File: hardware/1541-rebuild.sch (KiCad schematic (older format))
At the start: 12 parts, among them IC1 ATMEGA1284P-P, J1 ISP, J2 KEYS, J3 EXT_5V, J4 RESET CONN, J5 PC7, SW1 RESET, X1 24Mhz

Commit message: ERC Check Fehler behoben. GND + +5V PIN auf Power Out gestellt.
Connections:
- wire segments 125 -> 113
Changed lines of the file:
@@
 NoConn ~ 3600 3200
 $Comp
-L GND #PWR10
+L GND #PWR01
 U 1 1 55F7D4A6
 P 2000 3200
-F 0 "#PWR10" H 2000 2950 50  0001 C CNN
+F 0 "#PWR01" H 2000 2950 50  0001 C CNN
 F 1 "GND" H 2000 3050 50  0000 C CNN
 F 2 "" H 2000 3200 60  0000 C CNN
@@
 $EndComp
 $Comp
-L +5V #PWR8
+L +5V #PWR02
 U 1 1 55F7D4E4
 P 2000 2900
-F 0 "#PWR8" H 2000 2750 50  0001 C CNN
+F 0 "#PWR02" H 2000 2750 50  0001 C CNN
 F 1 "+5V" H 2000 3040 50  0000 C CNN
 F 2 "" H 2000 2900 60  0000 C CNN
@@
 NoConn ~ 4100 2500
 $Comp
-L GND #PWR13
+L GND #PWR03
 U 1 1 55F7EFD4
 P 5000 5950
-F 0 "#PWR13" H 5000 5700 50  0001 C CNN
+F 0 "#PWR03" H 5000 5700 50  0001 C CNN
 F 1 "GND" H 5000 5800 50  0000 C CNN
 F 2 "" H 5000 5950 60  0000 C CNN
@@
 $EndComp
 $Comp
-L +5V #PWR5
+L +5V #PWR04
 U 1 1 55F7F7C2
 P 5000 1650
-F 0 "#PWR5" H 5000 1500 50  0001 C CNN
+F 0 "#PWR04" H 5000 1500 50  0001 C CNN
 F 1 "+5V" H 5000 1790 50  0000 C CNN
 F 2 "" H 5000 1650 60  0000 C CNN
@@
 $EndComp
 $Comp
-L +5V #PWR7
+L +5V #PWR05
 U 1 1 55F7ED10
 P 3500 2100
-F 0 "#PWR7" H 3500 1950 50  0001 C CNN
+F 0 "#PWR05" H 3500 1950 50  0001 C CNN
 F 1 "+5V" H 3500 2240 50  0000 C CNN
 F 2 "" H 3500 2100 60  0000 C CNN
@@
 $EndComp
 $Comp
-L +5V #PWR3
+L +5V #PWR06
 U 1 1 55F800FF
 P 1500 1050
-F 0 "#PWR3" H 1500 900 50  0001 C CNN
+F 0 "#PWR06" H 1500 900 50  0001 C CNN
 F 1 "+5V" H 1500 1190 50  0000 C CNN
 F 2 "" H 1500 1050 60  0000 C CNN
@@
 $EndComp
 $Comp
-L GND #PWR2
+L GND #PWR07
 U 1 1 55F80221
 P 1200 1050
-F 0 "#PWR2" H 1200 800 50  0001 C CNN
+F 0 "#PWR07" H 1200 800 50  0001 C CNN
 F 1 "GND" H 1200 900 50  0000 C CNN
 F 2 "" H 1200 1050 60  0000 C CNN
@@
 $EndSheet
 Wire Wire Line
-	2000 2900 2100 2900
-Wire Wire Line
-	2100 2900 2200 2900
+	2000 2900 2200 2900
 Connection ~ 2100 2900
 Wire Wire Line
-	2000 3200 2100 3200
-Wire Wire Line
-	2100 3200 2200 3200
+	2000 3200 2200 3200
 Connection ~ 2100 3200
 Wire Wire Line
 	4900 5800 4900 5900
 Wire Wire Line
-	4900 5900 5000 5900
-Wire Wire Line
-	5000 5900 5100 5900
+	4900 5900 5100 5900
 Wire Wire Line
 	5000 5900 5000 5950
@@
 	4900 1800 4900 1700
 Wire Wire Line
-	4900 1700 5000 1700
-Wire Wire Line
-	5000 1700 5100 1700
+	4900 1700 5100 1700
 Wire Wire Line
 	5000 1700 5000 1650
@@
 	3650 2100 3500 2100
 Wire Wire Line
-	3950 2100 4050 2100
-Wire Wire Line
-	4050 2100 4100 2100
-Wire Wire Line
-	1200 1050 1200 1250
-Wire Wire Line
-	1200 1250 1200 1550
+	3950 2100 4100 2100
+Wire Wire Line
+	1200 1050 1200 1550
 Connection ~ 1200 1250
 Wire Wire Line
-	1500 1050 1500 1250
-Wire Wire Line
-	1500 1250 1500 1550
+	1500 1050 1500 1550
 Connection ~ 1500 1250
 Wire Wire Line
@@
 	6100 3400 7550 3400
 Wire Wire Line
-	6100 3500 7350 3500
-Wire Wire Line
-	7350 3500 7550 3500
-Wire Wire Line
-	6100 3600 7150 3600
-Wire Wire Line
-	7150 3600 7550 3600
-Wire Wire Line
-	6100 3700 7250 3700
-Wire Wire Line
-	7250 3700 7550 3700
+	6100 3500 7550 3500
+Wire Wire Line
+	6100 3600 7550 3600
+Wire Wire Line
+	6100 3700 7550 3700
 Wire Wire Line
 	6100 3300 6550 3300
@@
 	4050 2100 4050 1000
 Wire Wire Line
-	3950 1000 4050 1000
-Wire Wire Line
-	4050 1000 7400 1000
-Wire Wire Line
-	7400 1000 10650 1000
+	3950 1000 10650 1000
 Wire Wire Line
 	7400 1000 7400 1700
@@
 Connection ~ 4050 2100
 $Comp
-L +5V #PWR4
+L +5V #PWR08
 U 1 1 58409984
 P 8250 1450
-F 0 "#PWR4" H 8250 1300 50  0001 C CNN
+F 0 "#PWR08" H 8250 1300 50  0001 C CNN
 F 1 "+5V" H 8250 1590 50  0000 C CNN
 F 2 "" H 8250 1450 60  0000 C CNN
@@
 	8250 1500 8250 1450
 $Comp
-L GND #PWR6
+L GND #PWR09
 U 1 1 58409C3B
 P 8250 1750
-F 0 "#PWR6" H 8250 1500 50  0001 C CNN
+F 0 "#PWR09" H 8250 1500 50  0001 C CNN
 F 1 "GND" H 8250 1600 50  0000 C CNN
 F 2 "" H 8250 1750 60  0000 C CNN
@@
 Connection ~ 4050 1000
 $Comp
-L GND #PWR1
+L GND #PWR010
 U 1 1 5ADB9F66
 P 3100 1000
-F 0 "#PWR1" H 3100 1000 30  0001 C CNN
+F 0 "#PWR010" H 3100 1000 30  0001 C CNN
 F 1 "GND" H 3100 930 30  0001 C CNN
 F 2 "" H 3100 1000 60  0001 C CNN
@@
 $EndComp
 $Comp
-L GND #PWR9
+L GND #PWR011
 U 1 1 5AEE4F44
 P 9850 3150
-F 0 "#PWR9" H 9850 2900 50  0001 C CNN
+F 0 "#PWR011" H 9850 2900 50  0001 C CNN
 F 1 "GND" H 9850 3000 50  0000 C CNN
 F 2 "" H 9850 3150 60  0000 C CNN
@@
 $EndComp
 $Comp
-L GND #PWR12
+L GND #PWR012
 U 1 1 5AEF6E70
 P 1550 4700
-F 0 "#PWR12" H 1550 4450 50  0001 C CNN
+F 0 "#PWR012" H 1550 4450 50  0001 C CNN
 F 1 "GND" H 1550 4550 50  0000 C CNN
 F 2 "" H 1550 4700 60  0000 C CNN
@@
 $EndComp
 $Comp
-L +5V #PWR11
+L +5V #PWR013
 U 1 1 5AEF757D
 P 1250 4700
-F 0 "#PWR11" H 1250 4550 50  0001 C CNN
+F 0 "#PWR013" H 1250 4550 50  0001 C CNN
 F 1 "+5V" H 1250 4840 50  0000 C CNN
 F 2 "" H 1250 4700 60  0000 C CNN

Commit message: Allen Bauteilen Footprints zugeordnet.
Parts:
- J1: footprint (none) -> w_conn_strip:vasch_strip_3x2
- J2: footprint (none) -> Pin_Headers:Pin_Header_Straight_1x04_Pitch2.54mm
- J3, J4: footprint (none) -> Pin_Headers:Pin_Header_Straight_1x02_Pitch2.54mm
- J5: footprint (none) -> Pin_Headers:Pin_Header_Straight_1x01_Pitch2.54mm
- R1: footprint Resistors_ThroughHole:Resistor_Horizontal_RM10mm -> Discret:R4-5
- SW1: footprint Buttons_Switches_THT:SW_PUSH-12mm -> Buttons_Switches_THT:SW_PUSH_6mm_h5mm
- X1: footprint Oscillators:KXO-200_LargePads -> Oscillators:Oscillator_DIP-14_LargePads
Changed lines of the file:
@@
 F 0 "X1" H 2900 3350 70  0000 C CNN
 F 1 "24Mhz" H 2900 3050 70  0000 C CNN
-F 2 "Oscillators:KXO-200_LargePads" H 2900 3050 60  0001 C CNN
+F 2 "Oscillators:Oscillator_DIP-14_LargePads" H 2900 3050 60  0001 C CNN
 F 3 "" H 2900 3050 60  0000 C CNN
 	1    2900 3050
@@
 F 0 "R1" V 3880 2100 50  0000 C CNN
 F 1 "10k" V 3800 2100 50  0000 C CNN
-F 2 "Resistors_ThroughHole:Resistor_Horizontal_RM10mm" V 3730 2100 30  0001 C CNN
+F 2 "Discret:R4-5" V 3730 2100 30  0001 C CNN
 F 3 "" H 3800 2100 30  0000 C CNN
 	1    3800 2100
@@
 F 0 "SW1" H 3800 1110 50  0000 C CNN
 F 1 "RESET" H 3650 920 50  0000 C CNN
-F 2 "Buttons_Switches_THT:SW_PUSH-12mm" H 3650 1000 60  0001 C CNN
+F 2 "Buttons_Switches_THT:SW_PUSH_6mm_h5mm" H 3650 1000 60  0001 C CNN
 F 3 "" H 3650 1000 60  0000 C CNN
 	1    3650 1000
@@
 F 0 "J5" H 6200 6050 50  0000 C CNN
 F 1 "PC7" H 6200 5850 50  0000 C CNN
-F 2 "" H 6200 5950 50  0001 C CNN
+F 2 "Pin_Headers:Pin_Header_Straight_1x01_Pitch2.54mm" H 6200 5950 50  0001 C CNN
 F 3 "" H 6200 5950 50  0001 C CNN
 	1    6200 5950
@@
 F 0 "J2" H 10200 3150 50  0000 C CNN
 F 1 "KEYS" H 10200 2650 50  0000 C CNN
-F 2 "" H 10200 2950 50  0001 C CNN
+F 2 "Pin_Headers:Pin_Header_Straight_1x04_Pitch2.54mm" H 10200 2950 50  0001 C CNN
 F 3 "" H 10200 2950 50  0001 C CNN
 	1    10200 2950
@@
 F 0 "J1" H 7850 1800 50  0000 C CNN
 F 1 "ISP" H 7850 1400 50  0000 C CNN
-F 2 "" H 7800 1600 50  0001 C CNN
+F 2 "w_conn_strip:vasch_strip_3x2" H 7800 1600 50  0001 C CNN
 F 3 "" H 7800 1600 50  0001 C CNN
 	1    7800 1600
@@
 F 0 "J4" H 9400 4650 50  0000 C CNN
 F 1 "RESET CONN" H 9400 4350 50  0000 C CNN
-F 2 "" H 9400 4550 50  0001 C CNN
+F 2 "Pin_Headers:Pin_Header_Straight_1x02_Pitch2.54mm" H 9400 4550 50  0001 C CNN
 F 3 "" H 9400 4550 50  0001 C CNN
 	1    9400 4550
@@
 F 0 "J3" H 1350 4450 50  0000 C CNN
 F 1 "EXT_5V" H 1350 4150 50  0000 C CNN
-F 2 "" H 1350 4350 50  0001 C CNN
+F 2 "Pin_Headers:Pin_Header_Straight_1x02_Pitch2.54mm" H 1350 4350 50  0001 C CNN
 F 3 "" H 1350 4350 50  0001 C CNN
 	1    1350 4350

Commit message: - Hardware nochmal angepasst - erstes Layout erstellt - Schaltplan auf Rev.1.3.4 gesetzt
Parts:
- removed J5: PC7, Pin_Headers:Pin_Header_Straight_1x01_Pitch2.54mm, symbol Conn_01x01
- added J5: PC7, Pin_Headers:Pin_Header_Straight_1x02_Pitch2.54mm, symbol Conn_01x02
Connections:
- wire segments 113 -> 115
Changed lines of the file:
@@
 EESchema Schematic File Version 2
+LIBS:power
+LIBS:ka_library
 LIBS:1541-rebuild-rescue
-LIBS:power
 LIBS:device
 LIBS:transistors
@@
 LIBS:w_transistor
 LIBS:w_vacuum
-LIBS:kattanek
 LIBS:1541-rebuild-cache
 EELAYER 25 0
@@
 Sheet 1 4
 Title "1541-rebuid"
-Date "2018-05-06"
-Rev "1.3.3"
+Date "2018-05-08"
+Rev "1.3.4"
 Comp ""
 Comment1 "Erstellt von: Thorsten Kattanek"
@@
 NoConn ~ 3600 3200
 $Comp
-L GND #PWR01
-U 1 1 55F7D4A6
-P 2000 3200
-F 0 "#PWR01" H 2000 2950 50  0001 C CNN
-F 1 "GND" H 2000 3050 50  0000 C CNN
-F 2 "" H 2000 3200 60  0000 C CNN
-F 3 "" H 2000 3200 60  0000 C CNN
-	1    2000 3200
-	0    1    1    0
-$EndComp
-$Comp
-L +5V #PWR02
+L +5V #PWR01
 U 1 1 55F7D4E4
 P 2000 2900
-F 0 "#PWR02" H 2000 2750 50  0001 C CNN
+F 0 "#PWR01" H 2000 2750 50  0001 C CNN
 F 1 "+5V" H 2000 3040 50  0000 C CNN
 F 2 "" H 2000 2900 60  0000 C CNN
@@
 NoConn ~ 4100 2500
 $Comp
-L GND #PWR03
-U 1 1 55F7EFD4
-P 5000 5950
-F 0 "#PWR03" H 5000 5700 50  0001 C CNN
-F 1 "GND" H 5000 5800 50  0000 C CNN
-F 2 "" H 5000 5950 60  0000 C CNN
-F 3 "" H 5000 5950 60  0000 C CNN
-	1    5000 5950
-	1    0    0    -1
-$EndComp
-$Comp
-L +5V #PWR04
+L +5V #PWR02
 U 1 1 55F7F7C2
 P 5000 1650
-F 0 "#PWR04" H 5000 1500 50  0001 C CNN
+F 0 "#PWR02" H 5000 1500 50  0001 C CNN
 F 1 "+5V" H 5000 1790 50  0000 C CNN
 F 2 "" H 5000 1650 60  0000 C CNN
@@
 $EndComp
 $Comp
-L +5V #PWR05
+L +5V #PWR03
 U 1 1 55F7ED10
 P 3500 2100
-F 0 "#PWR05" H 3500 1950 50  0001 C CNN
+F 0 "#PWR03" H 3500 1950 50  0001 C CNN
 F 1 "+5V" H 3500 2240 50  0000 C CNN
 F 2 "" H 3500 2100 60  0000 C CNN
@@
 $EndComp
 $Comp
-L +5V #PWR06
+L +5V #PWR04
 U 1 1 55F800FF
 P 1500 1050
-F 0 "#PWR06" H 1500 900 50  0001 C CNN
+F 0 "#PWR04" H 1500 900 50  0001 C CNN
 F 1 "+5V" H 1500 1190 50  0000 C CNN
 F 2 "" H 1500 1050 60  0000 C CNN
@@
 	1    1500 1050
 	1    0    0    -1
-$EndComp
-$Comp
-L GND #PWR07
-U 1 1 55F80221
-P 1200 1050
-F 0 "#PWR07" H 1200 800 50  0001 C CNN
-F 1 "GND" H 1200 900 50  0000 C CNN
-F 2 "" H 1200 1050 60  0000 C CNN
-F 3 "" H 1200 1050 60  0000 C CNN
-	1    1200 1050
-	-1   0    0    1
 $EndComp
 Text Notes 750  750  0    60   ~ 0
@@
 Connection ~ 4050 2100
 $Comp
-L +5V #PWR08
+L +5V #PWR05
 U 1 1 58409984
 P 8250 1450
-F 0 "#PWR08" H 8250 1300 50  0001 C CNN
+F 0 "#PWR05" H 8250 1300 50  0001 C CNN
 F 1 "+5V" H 8250 1590 50  0000 C CNN
 F 2 "" H 8250 1450 60  0000 C CNN
@@
 Wire Wire Line
 	8250 1500 8250 1450
-$Comp
-L GND #PWR09
-U 1 1 58409C3B
-P 8250 1750
-F 0 "#PWR09" H 8250 1500 50  0001 C CNN
-F 1 "GND" H 8250 1600 50  0000 C CNN
-F 2 "" H 8250 1750 60  0000 C CNN
-F 3 "" H 8250 1750 60  0000 C CNN
-	1    8250 1750
-	1    0    0    -1
-$EndComp
 Wire Wire Line
 	8100 1700 8250 1700
@@
 Connection ~ 7350 3500
 Wire Wire Line
-	6200 4600 6200 5750
-Wire Wire Line
-	6200 4600 6100 4600
+	6100 4600 6250 4600
 Wire Wire Line
 	10650 1000 10650 4900
@@
 $EndComp
 Connection ~ 4050 1000
-$Comp
-L GND #PWR010
-U 1 1 5ADB9F66
-P 3100 1000
-F 0 "#PWR010" H 3100 1000 30  0001 C CNN
-F 1 "GND" H 3100 930 30  0001 C CNN
-F 2 "" H 3100 1000 60  0001 C CNN
-F 3 "" H 3100 1000 60  0001 C CNN
-	1    3100 1000
-	0    1    1    0
-$EndComp
 Wire Wire Line
 	3100 1000 3350 1000
-$Comp
-L Conn_01x01 J5
-U 1 1 5AED8BA4
-P 6200 5950
-F 0 "J5" H 6200 6050 50  0000 C CNN
-F 1 "PC7" H 6200 5850 50  0000 C CNN
-F 2 "Pin_Headers:Pin_Header_Straight_1x01_Pitch2.54mm" H 6200 5950 50  0001 C CNN
-F 3 "" H 6200 5950 50  0001 C CNN
-	1    6200 5950
-	0    1    1    0
-$EndComp
 $Comp
 L Conn_01x04 J2
@@
 	1    10200 2950
 	1    0    0    -1
-$EndComp
-$Comp
-L GND #PWR011
-U 1 1 5AEE4F44
-P 9850 3150
-F 0 "#PWR011" H 9850 2900 50  0001 C CNN
-F 1 "GND" H 9850 3000 50  0000 C CNN
-F 2 "" H 9850 3150 60  0000 C CNN
-F 3 "" H 9850 3150 60  0000 C CNN
-	1    9850 3150
-	0    1    1    0
 $EndComp
 Wire Wire Line
@@
 $EndComp
 $Comp
-L GND #PWR012
-U 1 1 5AEF6E70
-P 1550 4700
-F 0 "#PWR012" H 1550 4450 50  0001 C CNN
-F 1 "GND" H 1550 4550 50  0000 C CNN
-F 2 "" H 1550 4700 60  0000 C CNN
-F 3 "" H 1550 4700 60  0000 C CNN
-	1    1550 4700
-	0    -1   -1   0
-$EndComp
-$Comp
-L +5V #PWR013
+L +5V #PWR06
 U 1 1 5AEF757D
 P 1250 4700
-F 0 "#PWR013" H 1250 4550 50  0001 C CNN
+F 0 "#PWR06" H 1250 4550 50  0001 C CNN
 F 1 "+5V" H 1250 4840 50  0000 C CNN
 F 2 "" H 1250 4700 60  0000 C CNN
@@
 Wire Wire Line
 	3600 2900 4100 2900
+$Comp
+L GND #PWR07
+U 1 1 5AF09AC0
+P 1200 1050
+F 0 "#PWR07" H 1200 800 50  0001 C CNN
+F 1 "GND" H 1200 900 50  0000 C CNN
+F 2 "" H 1200 1050 50  0001 C CNN
+F 3 "" H 1200 1050 50  0001 C CNN
+	1    1200 1050
+	-1   0    0    1
+$EndComp
+$Comp
+L GND #PWR08
+U 1 1 5AF09DC8
+P 3100 1000
+F 0 "#PWR08" H 3100 750 50  0001 C CNN
+F 1 "GND" H 3100 850 50  0000 C CNN
+F 2 "" H 3100 1000 50  0001 C CNN
+F 3 "" H 3100 1000 50  0001 C CNN
+	1    3100 1000
+	0    1    1    0
+$EndComp
+$Comp
+L GND #PWR09
+U 1 1 5AF0A3CF
+P 2000 3200
+F 0 "#PWR09" H 2000 2950 50  0001 C CNN
+F 1 "GND" H 2000 3050 50  0000 C CNN
+F 2 "" H 2000 3200 50  0001 C CNN
+F 3 "" H 2000 3200 50  0001 C CNN
+	1    2000 3200
+	0    1    1    0
+$EndComp
+$Comp
+L GND #PWR010
+U 1 1 5AF0A9E7
+P 1550 4700
+F 0 "#PWR010" H 1550 4450 50  0001 C CNN
+F 1 "GND" H 1550 4550 50  0000 C CNN
+F 2 "" H 1550 4700 50  0001 C CNN
+F 3 "" H 1550 4700 50  0001 C CNN
+	1    1550 4700
+	0    -1   -1   0
+$EndComp
+$Comp
+L GND #PWR011
+U 1 1 5AF0ADEC
+P 5000 5950
+F 0 "#PWR011" H 5000 5700 50  0001 C CNN
+F 1 "GND" H 5000 5800 50  0000 C CNN
+F 2 "" H 5000 5950 50  0001 C CNN
+F 3 "" H 5000 5950 50  0001 C CNN
+	1    5000 5950
+	1    0    0    -1
+$EndComp
+$Comp
+L GND #PWR012
+U 1 1 5AF0B2ED
+P 8250 1750
+F 0 "#PWR012" H 8250 1500 50  0001 C CNN
+F 1 "GND" H 8250 1600 50  0000 C CNN
+F 2 "" H 8250 1750 50  0001 C CNN
+F 3 "" H 8250 1750 50  0001 C CNN
+	1    8250 1750
+	1    0    0    -1
+$EndComp
+$Comp
+L GND #PWR013
+U 1 1 5AF0B7EE
+P 9850 3150
+F 0 "#PWR013" H 9850 2900 50  0001 C CNN
+F 1 "GND" H 9850 3000 50  0000 C CNN
+F 2 "" H 9850 3150 50  0001 C CNN
+F 3 "" H 9850 3150 50  0001 C CNN
+	1    9850 3150
+	0    1    1    0
+$EndComp
+$Comp
+L Conn_01x02 J5
+U 1 1 5AF1C880
+P 6250 6200
+F 0 "J5" H 6250 6300 50  0000 C CNN
+F 1 "PC7" H 6250 6000 50  0000 C CNN
+F 2 "Pin_Headers:Pin_Header_Straight_1x02_Pitch2.54mm" H 6250 6200 50  0001 C CNN
+F 3 "" H 6250 6200 50  0001 C CNN
+	1    6250 6200
+	0    1    1    0
+$EndComp
+Wire Wire Line
+	6250 4600 6250 6000
+$Comp
+L GND #PWR014
+U 1 1 5AF1E3E7
+P 6050 5950
+F 0 "#PWR014" H 6050 5700 50  0001 C CNN
+F 1 "GND" H 6050 5800 50  0000 C CNN
+F 2 "" H 6050 5950 50  0001 C CNN
+F 3 "" H 6050 5950 50  0001 C CNN
+	1    6050 5950
+	0    1    1    0
+$EndComp
+Wire Wire Line
+	6050 5950 6150 5950
+Wire Wire Line
+	6150 5950 6150 6000
 $EndSCHEMATC

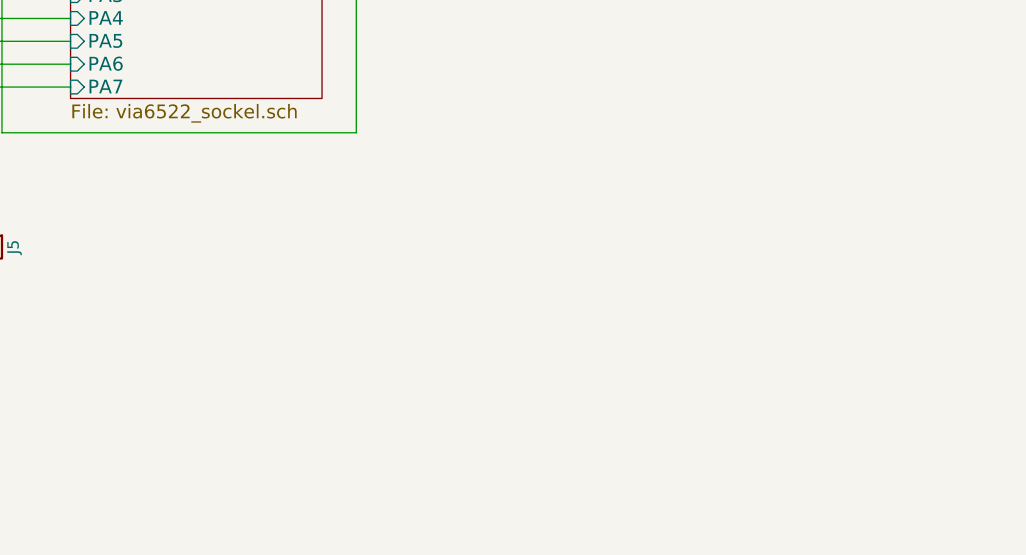
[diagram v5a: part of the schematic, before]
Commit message: Bezugsquellen für den SD Slot im Schaltplan hinzugefügt.
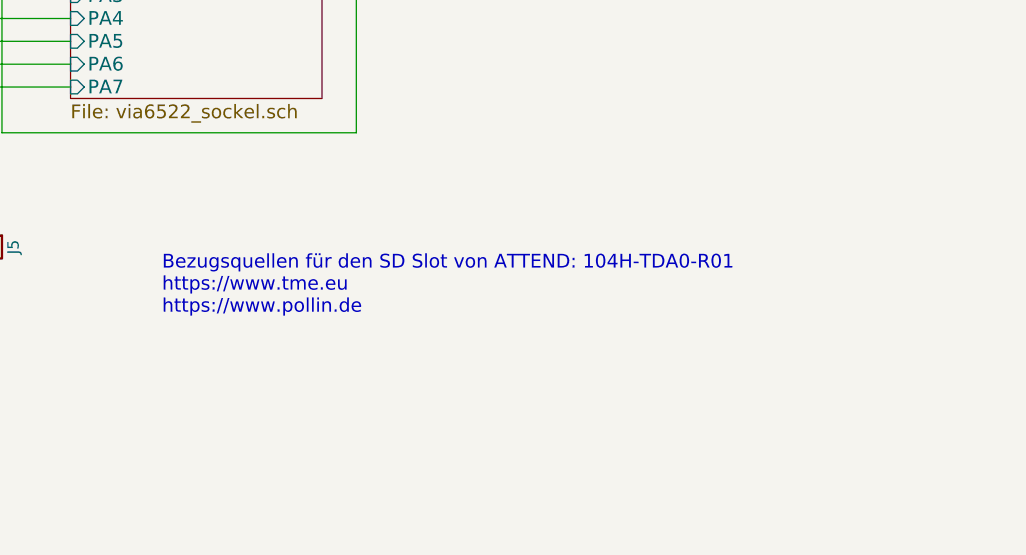
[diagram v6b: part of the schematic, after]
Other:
- note added: "Bezugsquellen für den SD Slot von ATTEND: 104H-TDA0-R01\nhttps://www.tme.eu\nhttps://www.pollin.de\n"
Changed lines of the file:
@@
 Sheet 1 4
 Title "1541-rebuid"
-Date "2018-05-11"
+Date "2018-05-16"
 Rev "1.3.5"
 Comp ""
@@
 Wire Wire Line
 	6150 5950 6150 6000
+Text Notes 7000 6500 0    60   ~ 0
+Bezugsquellen für den SD Slot von ATTEND: 104H-TDA0-R01\nhttps://www.tme.eu\nhttps://www.pollin.de\n
 $EndSCHEMATC

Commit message: Hardware Projekt knovertiert von KiCad 4 -> KiCad 5 - Schaltplan angepasst - neues Detailfoto hinzugefügt - Footprints neu zugeordnet, somit ist auch wieder eine 3D Darstellung möglich - Readme.md angepasst
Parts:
- C1, C2, C3: footprint w_capacitors:cnp_3mm_disc -> Capacitor_THT:C_Disc_D5.1mm_W3.2mm_P5.00mm; symbol C -> Device:C
- IC1: footprint w_pth_circuits:dil_40-600_socket -> Package_DIP:DIP-40_W15.24mm_Socket_LongPads; symbol ATMEGA1284P-P -> MCU_Microchip_ATmega:ATmega1284P-PU
- J1: footprint w_conn_strip:vasch_strip_3x2 -> Connector_IDC:IDC-Header_2x03_P2.54mm_Vertical; symbol Conn_02x03_Odd_Even -> Connector_Generic:Conn_02x03_Odd_Even
- J2: footprint Pin_Headers:Pin_Header_Straight_1x04_Pitch2.54mm -> Connector_PinHeader_2.54mm:PinHeader_1x04_P2.54mm_Vertical; symbol Conn_01x04 -> Connector_Generic:Conn_01x04
- J3, J4, J5: footprint Pin_Headers:Pin_Header_Straight_1x02_Pitch2.54mm -> Connector_PinHeader_2.54mm:PinHeader_1x02_P2.54mm_Vertical; symbol Conn_01x02 -> Connector_Generic:Conn_01x02
- R1: footprint Discret:R4-5 -> Resistor_THT:R_Axial_DIN0207_L6.3mm_D2.5mm_P10.16mm_Horizontal; symbol R -> Device:R
- SW1: footprint Buttons_Switches_THT:SW_PUSH_6mm_h5mm -> Button_Switch_THT:SW_PUSH_6mm_H5mm; symbol SW_PUSH-RESCUE-1541-rebuild -> Switch:SW_Push
- X1: footprint Oscillators:Oscillator_DIP-14_LargePads -> Oscillator:Oscillator_DIP-14_LargePads; symbol TCXO3-RESCUE-1541-rebuild -> Oscillator:TCXO-14
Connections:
- net LCD Display/D0 renamed LCD Display/D4
- net LCD Display/D1 renamed LCD Display/D5
- net LCD Display/D2 renamed LCD Display/D6
- net LCD Display/D3 renamed LCD Display/D7
- no-connect marks 3 -> 2
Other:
- note added: "Am meiner 1541II Platine (ASSY NO 345003 REV 9) habe ich folgende modifiktionen durchgeführt:\n- PIN 42 von U10 (Gate Array 251828) von Platine getrennt (BYTE READY)\n- U8 (VIA 6522) ausgelötet und gesockelt\n- Dauerläufer behoben durch trennen einer Leiterbahn zwischen R/W Amp Pin 32 (Power On) und den 220 Ohm Widerstand"
- note removed: "Am meiner 1541II Platine (ASSY NO 345003 REV 9) habe ich folgende modifiktionen durchgeführt:\n- PIN 40 von U10 (Gate Array 251828) von Platine getrennt (BYTE READY)\n- U8 (VIA 6522) ausgelötet und gesockelt\n- Dauerläufer behoben durch trennen einer Leiterbahn (genauer beschreiben)"
- moved on the sheet: C3
